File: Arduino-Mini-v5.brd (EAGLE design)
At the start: 17.8 x 30.5 mm, 35 parts, among them IC1 LP2985AIM5-5.0, SW1 RESET, U1 ATMEGA328P-MU, X2 16MHz

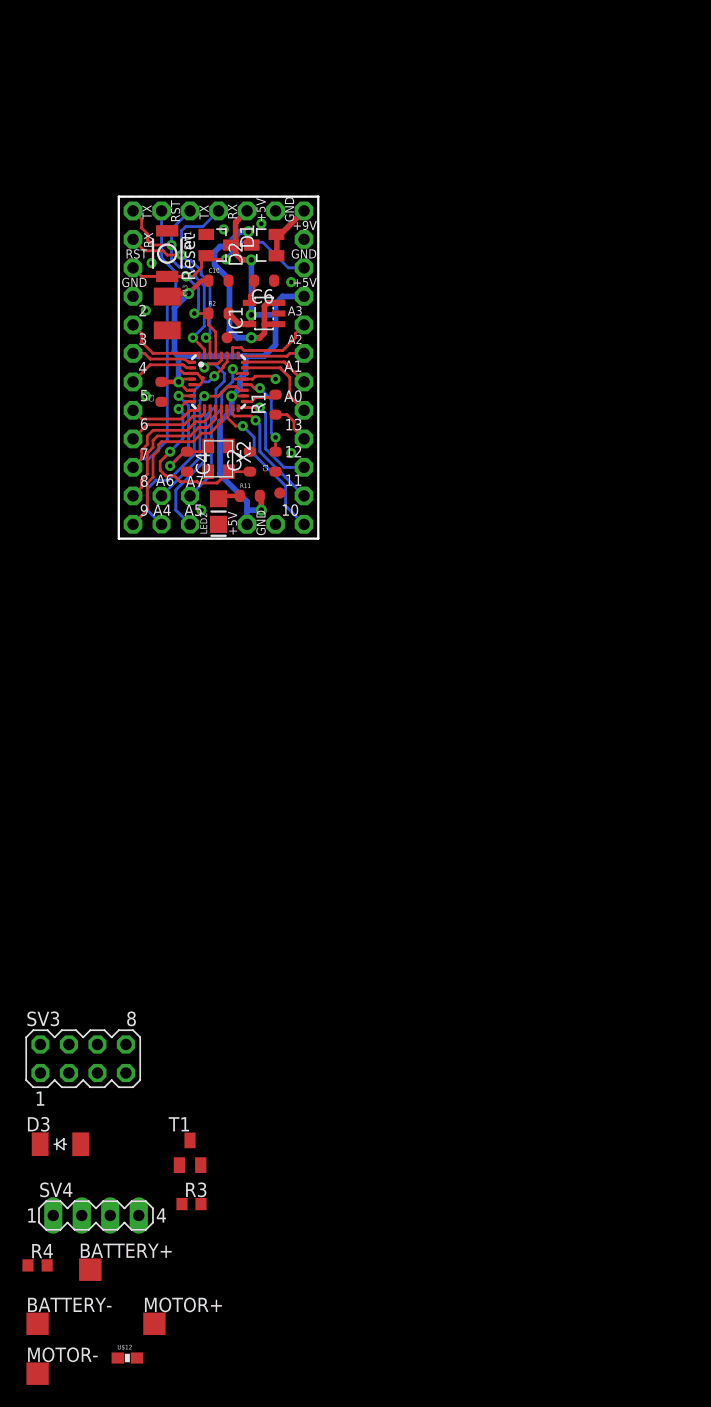
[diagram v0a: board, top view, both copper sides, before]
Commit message: placed parts, no routes
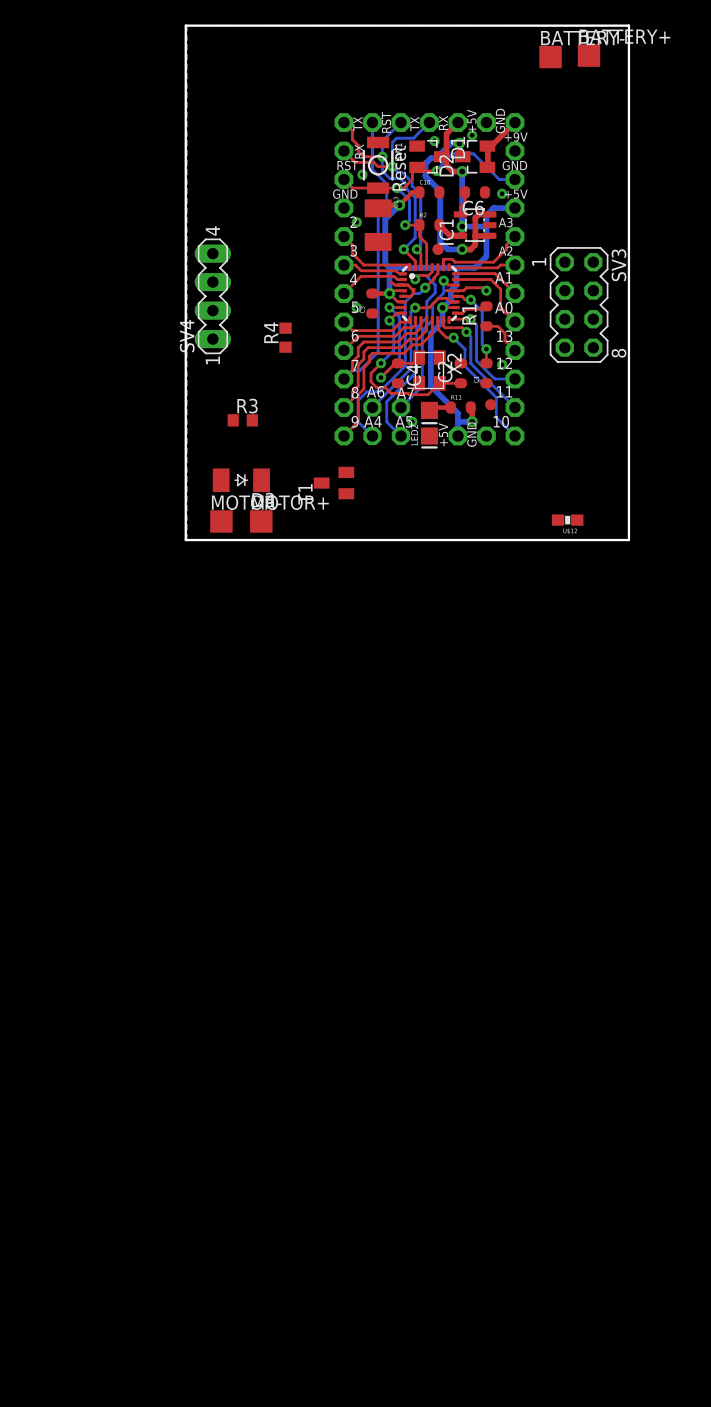
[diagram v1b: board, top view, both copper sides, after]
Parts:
- moved BATTERY- 121.8 mm to (38.5, 42.9)
- moved BATTERY+ 117.0 mm to (41.9, 43.1)
- moved R4 85.6 mm to (14.9, 17.9), turned to 90 degrees
- moved U$12 84.4 mm to (40.0, 1.65), turned to 180 degrees
- moved SV4 82.6 mm to (8.38, 21.6), turned to 90 degrees
- moved SV3 80.4 mm to (41.0, 20.8), turned to 270 degrees
- moved MOTOR- 77.7 mm to (9.14, 1.52)
- moved MOTOR+ 72.1 mm to (12.7, 1.52)
- moved R3 70.0 mm to (11.0, 10.5)
- moved D3 61.3 mm to (10.9, 5.21), turned to 180 degrees
- moved T1 61.1 mm to (19.2, 4.95), turned to 90 degrees
- moved C3 20.4 mm to (22.6, 21.0)
- moved C1 20.4 mm to (32.8, 14.7)
- moved C10 20.4 mm to (27.7, 30.9)
- moved C13 20.4 mm to (23.1, 27.9)
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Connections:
- net +5V: now also D3.C
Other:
- board size 17.8 x 30.5 mm -> 39.5 x 45.8 mm

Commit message: routed 100% :)
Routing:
- net IO8: track 13.0 -> 72.5 mm
- net +5V: track 71.0 -> 130.4 mm
- net IO7: track 35.7 -> 85.6 mm
- net ADC0: track 7.81 -> 27.8 mm
- net IO4: track 5.99 -> 24.6 mm
- net +VID: track 27.5 -> 45.9 mm
- net N$14: track 0.00 -> 16.7 mm
- net IO3: track 5.57 -> 18.9 mm
- net N$13: track 0.00 -> 12.9 mm
- net VCC: track 6.03 -> 15.1 mm
- net IO5: track 6.67 -> 12.1 mm

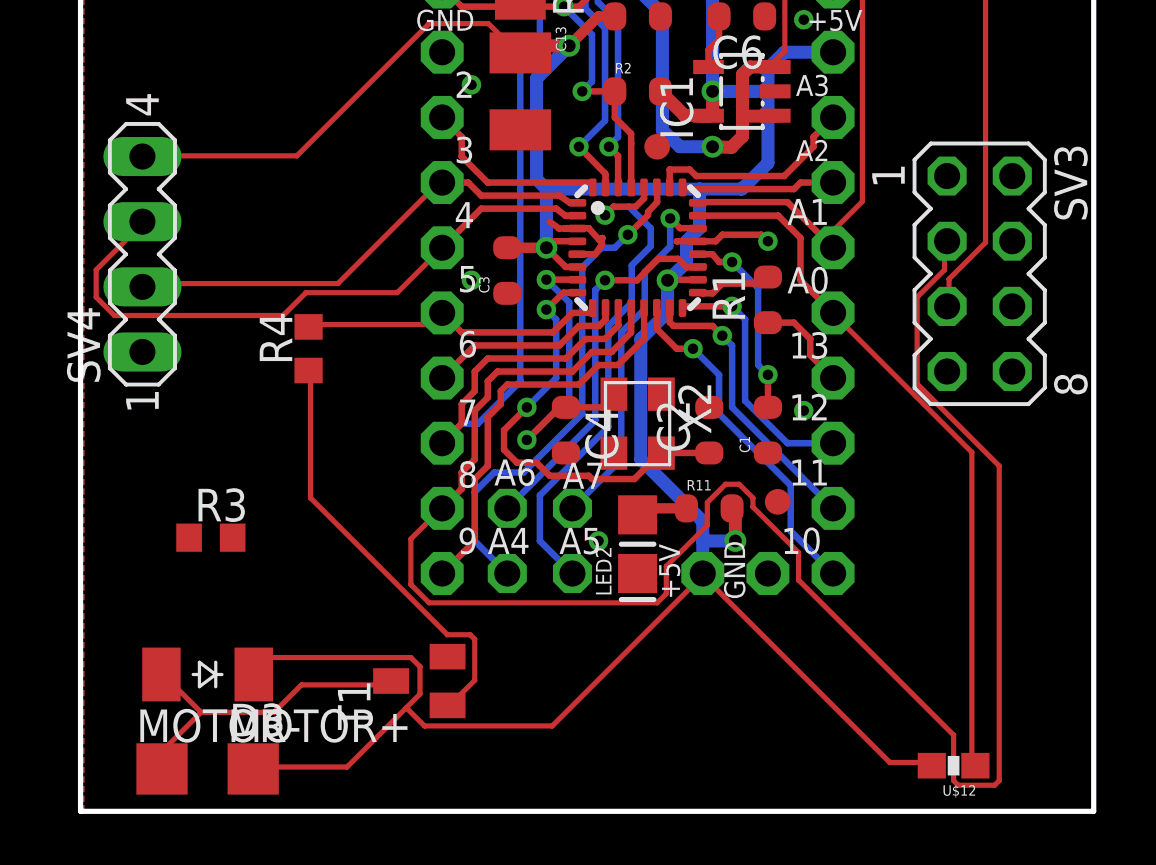
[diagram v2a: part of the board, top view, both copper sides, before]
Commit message: fixing the thermister flaw
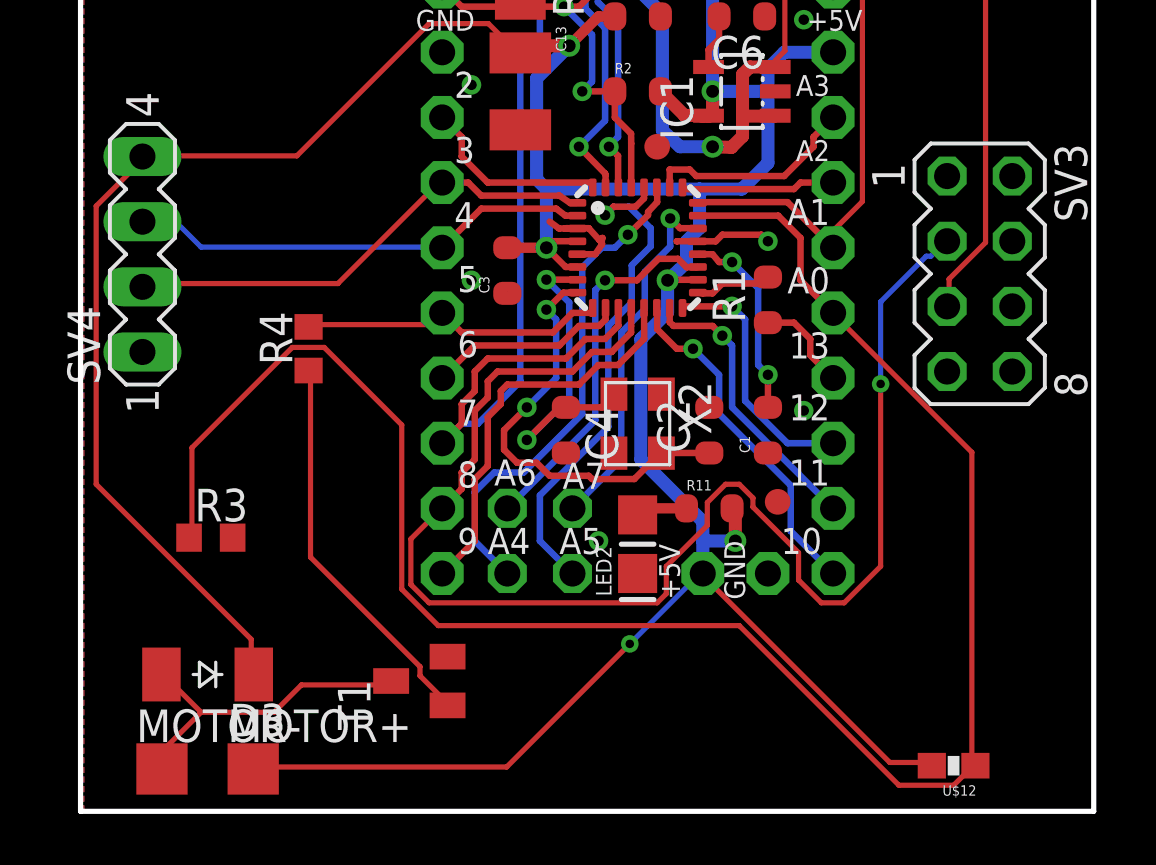
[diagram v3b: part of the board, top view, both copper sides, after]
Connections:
- net ADC0: now also R3.1
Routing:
- net ADC0: track 27.8 -> 74.6 mm
- net IO8: track 72.5 -> 55.4 mm, vias 0 -> 1
- net +5V: track 130.4 -> 144.5 mm, vias 6 -> 7
- net IO4: track 24.6 -> 18.1 mm
- net N$14: track 16.7 -> 15.3 mm
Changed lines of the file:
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@@
 <contactref element="BATTERY-" pad="TP"/>
 <wire x1="20.277" y1="5.903" x2="26.162" y2="10.414" width="0" layer="19" extent="1-1"/>
+<wire x1="11.899" y1="10.541" x2="8.382" y2="17.78" width="0" layer="19" extent="1-1"/>
 </signal>
 <signal name="AREF">
@@
 <wire x1="27.432" y1="18.796" x2="27.436" y2="19.494" width="0.254" layer="1"/>
 <contactref element="SV3" pad="3"/>
-<wire x1="39.6494" y1="20.9804" x2="39.6494" y2="22.0472" width="0.2032" layer="1"/>
-<wire x1="38.5826" y1="19.9136" x2="39.6494" y2="20.9804" width="0.2032" layer="1"/>
-<wire x1="38.5826" y1="16.5354" x2="38.5826" y2="19.9136" width="0.2032" layer="1"/>
-<wire x1="41.783" y1="13.335" x2="38.5826" y2="16.5354" width="0.2032" layer="1"/>
-<wire x1="41.783" y1="1.0668" x2="41.783" y2="13.335" width="0.2032" layer="1"/>
-<wire x1="41.6052" y1="0.889" x2="41.783" y2="1.0668" width="0.2032" layer="1"/>
-<wire x1="40.1828" y1="0.889" x2="41.6052" y2="0.889" width="0.2032" layer="1"/>
-<wire x1="40.005" y1="1.0668" x2="40.1828" y2="0.889" width="0.2032" layer="1"/>
-<wire x1="40.005" y1="2.8448" x2="40.005" y2="1.0668" width="0.2032" layer="1"/>
-<wire x1="33.9598" y1="8.89" x2="40.005" y2="2.8448" width="0.2032" layer="1"/>
+<wire x1="39.116" y1="21.5138" x2="39.6494" y2="22.0472" width="0.2032" layer="16"/>
+<wire x1="38.9382" y1="21.5138" x2="39.116" y2="21.5138" width="0.2032" layer="16"/>
+<wire x1="37.1602" y1="19.7358" x2="38.9382" y2="21.5138" width="0.2032" layer="16"/>
+<wire x1="37.1602" y1="16.5354" x2="37.1602" y2="19.7358" width="0.2032" layer="16"/>
+<wire x1="37.1602" y1="9.4234" x2="37.1602" y2="16.5354" width="0.2032" layer="1"/>
+<wire x1="35.7378" y1="8.001" x2="37.1602" y2="9.4234" width="0.2032" layer="1"/>
+<wire x1="34.8488" y1="8.001" x2="35.7378" y2="8.001" width="0.2032" layer="1"/>
+<wire x1="33.9598" y1="8.89" x2="34.8488" y2="8.001" width="0.2032" layer="1"/>
 <wire x1="33.9598" y1="9.9568" x2="33.9598" y2="8.89" width="0.2032" layer="1"/>
 <wire x1="32.1818" y1="11.7348" x2="33.9598" y2="9.9568" width="0.2032" layer="1"/>
@@
 <wire x1="18.8468" y1="10.4902" x2="18.8468" y2="8.7122" width="0.2032" layer="1"/>
 <wire x1="19.9136" y1="11.557" x2="18.8468" y2="10.4902" width="0.2032" layer="1"/>
-<wire x1="39.6494" y1="22.0472" x2="39.751" y2="22.098" width="0.2032" layer="1"/>
+<wire x1="39.6494" y1="22.0472" x2="39.751" y2="22.098" width="0.2032" layer="16"/>
 <wire x1="19.9136" y1="11.557" x2="20.066" y2="11.684" width="0.2032" layer="1"/>
+<via x="37.1602" y="16.5354" extent="1-16" drill="0.3302" shape="octagon"/>
 </signal>
 <signal name="ADC5">
@@
 <wire x1="34.036" y1="20.574" x2="35.306" y2="19.304" width="0.254" layer="1"/>
 <contactref element="U$12" pad="1"/>
-<wire x1="40.7162" y1="13.8684" x2="40.7162" y2="1.778" width="0.2032" layer="1"/>
-<wire x1="35.3822" y1="19.2024" x2="40.7162" y2="13.8684" width="0.2032" layer="1"/>
+<contactref element="R3" pad="1"/>
+<wire x1="10.3124" y1="14.0462" x2="10.3124" y2="10.668" width="0.2032" layer="1"/>
+<wire x1="14.224" y1="17.9578" x2="10.3124" y2="14.0462" width="0.2032" layer="1"/>
+<wire x1="15.4686" y1="17.9578" x2="14.224" y2="17.9578" width="0.2032" layer="1"/>
+<wire x1="18.4912" y1="14.9352" x2="15.4686" y2="17.9578" width="0.2032" layer="1"/>
+<wire x1="18.4912" y1="8.5344" x2="18.4912" y2="14.9352" width="0.2032" layer="1"/>
+<wire x1="19.9136" y1="7.112" x2="18.4912" y2="8.5344" width="0.2032" layer="1"/>
+<wire x1="31.6484" y1="7.112" x2="19.9136" y2="7.112" width="0.2032" layer="1"/>
+<wire x1="37.8714" y1="0.889" x2="31.6484" y2="7.112" width="0.2032" layer="1"/>
+<wire x1="40.005" y1="0.889" x2="37.8714" y2="0.889" width="0.2032" layer="1"/>
+<wire x1="40.7162" y1="1.6002" x2="40.005" y2="0.889" width="0.2032" layer="1"/>
+<wire x1="10.3124" y1="10.668" x2="10.199" y2="10.541" width="0.2032" layer="1"/>
+<wire x1="40.7162" y1="1.6002" x2="40.855" y2="1.651" width="0.2032" layer="1"/>
+<wire x1="40.7162" y1="13.8684" x2="35.3822" y2="19.2024" width="0.2032" layer="1"/>
+<wire x1="40.7162" y1="1.778" x2="40.7162" y2="13.8684" width="0.2032" layer="1"/>
+<wire x1="35.3822" y1="19.2024" x2="35.306" y2="19.304" width="0.2032" layer="1"/>
 <wire x1="40.7162" y1="1.778" x2="40.855" y2="1.651" width="0.2032" layer="1"/>
-<wire x1="35.3822" y1="19.2024" x2="35.306" y2="19.304" width="0.2032" layer="1"/>
 </signal>
 <signal name="IO7">
@@
 <wire x1="21.59" y1="23.368" x2="20.066" y2="21.844" width="0.254" layer="1"/>
 <contactref element="SV4" pad="3"/>
-<wire x1="6.5786" y1="20.9804" x2="8.3566" y2="22.7584" width="0.2032" layer="1"/>
-<wire x1="6.5786" y1="19.9136" x2="6.5786" y2="20.9804" width="0.2032" layer="1"/>
-<wire x1="7.2898" y1="19.2024" x2="6.5786" y2="19.9136" width="0.2032" layer="1"/>
-<wire x1="13.8684" y1="19.2024" x2="7.2898" y2="19.2024" width="0.2032" layer="1"/>
-<wire x1="14.7574" y1="20.0914" x2="13.8684" y2="19.2024" width="0.2032" layer="1"/>
-<wire x1="18.3134" y1="20.0914" x2="14.7574" y2="20.0914" width="0.2032" layer="1"/>
-<wire x1="20.066" y1="21.844" x2="18.3134" y2="20.0914" width="0.2032" layer="1"/>
-<wire x1="8.3566" y1="22.7584" x2="8.382" y2="22.86" width="0.2032" layer="1"/>
+<wire x1="9.779" y1="22.7584" x2="8.5344" y2="22.7584" width="0.2032" layer="16"/>
+<wire x1="10.668" y1="21.8694" x2="9.779" y2="22.7584" width="0.2032" layer="16"/>
+<wire x1="19.9136" y1="21.8694" x2="10.668" y2="21.8694" width="0.2032" layer="16"/>
+<wire x1="8.5344" y1="22.7584" x2="8.382" y2="22.86" width="0.2032" layer="16"/>
+<wire x1="19.9136" y1="21.8694" x2="20.066" y2="21.844" width="0.2032" layer="16"/>
 </signal>
 <signal name="IO5">
@@
 <contactref element="MOTOR+" pad="TP"/>
 <contactref element="D3" pad="C"/>
-<wire x1="16.3576" y1="1.6002" x2="12.8016" y2="1.6002" width="0.2032" layer="1"/>
-<wire x1="19.2024" y1="4.445" x2="18.669" y2="3.9116" width="0.2032" layer="1"/>
-<wire x1="18.669" y1="3.9116" x2="16.3576" y2="1.6002" width="0.2032" layer="1"/>
-<wire x1="19.2024" y1="5.5118" x2="19.2024" y2="4.445" width="0.2032" layer="1"/>
-<wire x1="18.8468" y1="5.8674" x2="19.2024" y2="5.5118" width="0.2032" layer="1"/>
-<wire x1="13.335" y1="5.8674" x2="18.8468" y2="5.8674" width="0.2032" layer="1"/>
-<wire x1="12.8016" y1="5.334" x2="13.335" y2="5.8674" width="0.2032" layer="1"/>
-<wire x1="12.8016" y1="1.6002" x2="12.7" y2="1.524" width="0.2032" layer="1"/>
-<wire x1="12.8016" y1="5.334" x2="12.722" y2="5.207" width="0.2032" layer="1"/>
+<wire x1="12.6238" y1="6.5786" x2="12.6238" y2="5.334" width="0.2032" layer="1"/>
+<wire x1="6.5786" y1="12.6238" x2="12.6238" y2="6.5786" width="0.2032" layer="1"/>
+<wire x1="6.5786" y1="23.4696" x2="6.5786" y2="12.6238" width="0.2032" layer="1"/>
+<wire x1="8.3566" y1="25.2476" x2="6.5786" y2="23.4696" width="0.2032" layer="1"/>
+<wire x1="12.6238" y1="5.334" x2="12.722" y2="5.207" width="0.2032" layer="1"/>
+<wire x1="8.3566" y1="25.2476" x2="8.382" y2="25.4" width="0.2032" layer="1"/>
 <wire x1="37.5158" y1="1.778" x2="39.116" y2="1.778" width="0.2032" layer="1"/>
 <wire x1="30.226" y1="9.0678" x2="37.5158" y2="1.778" width="0.2032" layer="1"/>
 <wire x1="39.116" y1="1.778" x2="39.155" y2="1.651" width="0.2032" layer="1"/>
+<wire x1="30.226" y1="9.0678" x2="30.226" y2="9.144" width="0.2032" layer="1"/>
+<wire x1="22.5806" y1="1.6002" x2="12.8016" y2="1.6002" width="0.2032" layer="1"/>
+<wire x1="27.3812" y1="6.4008" x2="22.5806" y2="1.6002" width="0.2032" layer="1"/>
+<wire x1="30.0482" y1="9.0678" x2="27.3812" y2="6.4008" width="0.2032" layer="16"/>
+<wire x1="12.8016" y1="1.6002" x2="12.7" y2="1.524" width="0.2032" layer="1"/>
+<wire x1="30.0482" y1="9.0678" x2="30.226" y2="9.144" width="0.2032" layer="16"/>
 <wire x1="14.4018" y1="25.4254" x2="8.5344" y2="25.4254" width="0.2032" layer="1"/>
 <wire x1="19.558" y1="30.5816" x2="14.4018" y2="25.4254" width="0.2032" layer="1"/>
@@
 <wire x1="8.5344" y1="25.4254" x2="8.382" y2="25.4" width="0.2032" layer="1"/>
 <wire x1="22.9362" y1="29.5148" x2="23.114" y2="29.44" width="0.2032" layer="1"/>
-<wire x1="19.3802" y1="3.2004" x2="18.669" y2="3.9116" width="0.2032" layer="1"/>
-<wire x1="24.3586" y1="3.2004" x2="19.3802" y2="3.2004" width="0.2032" layer="1"/>
-<wire x1="30.226" y1="9.0678" x2="24.3586" y2="3.2004" width="0.2032" layer="1"/>
-<wire x1="30.226" y1="9.0678" x2="30.226" y2="9.144" width="0.2032" layer="1"/>
+<via x="27.3812" y="6.4008" extent="1-16" drill="0.3302" shape="octagon"/>
 </signal>
 <signal name="N$4">
@@
 <contactref element="T1" pad="B"/>
 <contactref element="R4" pad="1"/>
-<wire x1="14.9352" y1="12.0904" x2="14.9352" y2="16.891" width="0.2032" layer="1"/>
-<wire x1="20.2692" y1="6.7564" x2="14.9352" y2="12.0904" width="0.2032" layer="1"/>
-<wire x1="21.1582" y1="6.7564" x2="20.2692" y2="6.7564" width="0.2032" layer="1"/>
-<wire x1="21.336" y1="6.5786" x2="21.1582" y2="6.7564" width="0.2032" layer="1"/>
-<wire x1="21.336" y1="4.9784" x2="21.336" y2="6.5786" width="0.2032" layer="1"/>
-<wire x1="20.447" y1="4.0894" x2="21.336" y2="4.9784" width="0.2032" layer="1"/>
+<wire x1="14.9352" y1="9.779" x2="14.9352" y2="16.891" width="0.2032" layer="1"/>
+<wire x1="19.2024" y1="5.5118" x2="14.9352" y2="9.779" width="0.2032" layer="1"/>
+<wire x1="19.2024" y1="5.1562" x2="19.2024" y2="5.5118" width="0.2032" layer="1"/>
+<wire x1="20.2692" y1="4.0894" x2="19.2024" y2="5.1562" width="0.2032" layer="1"/>
 <wire x1="14.9352" y1="16.891" x2="14.859" y2="17.057" width="0.2032" layer="1"/>
-<wire x1="20.447" y1="4.0894" x2="20.277" y2="4.003" width="0.2032" layer="1"/>
+<wire x1="20.2692" y1="4.0894" x2="20.277" y2="4.003" width="0.2032" layer="1"/>
 </signal>
 </signals>
